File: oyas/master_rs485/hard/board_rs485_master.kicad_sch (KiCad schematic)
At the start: 0 parts

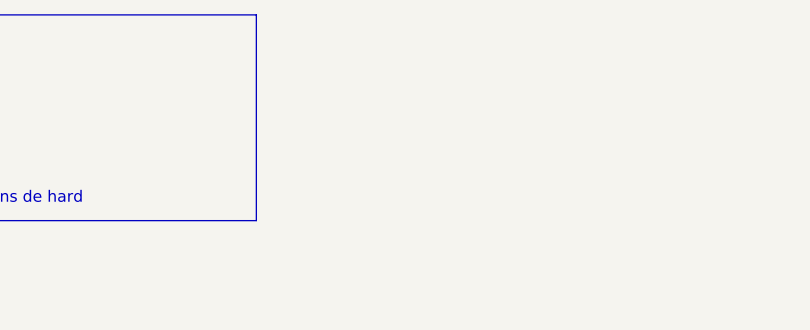
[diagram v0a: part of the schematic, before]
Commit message: MAJ correction limitation du courant de base des pnp (Pwr Wifi et LEDs)
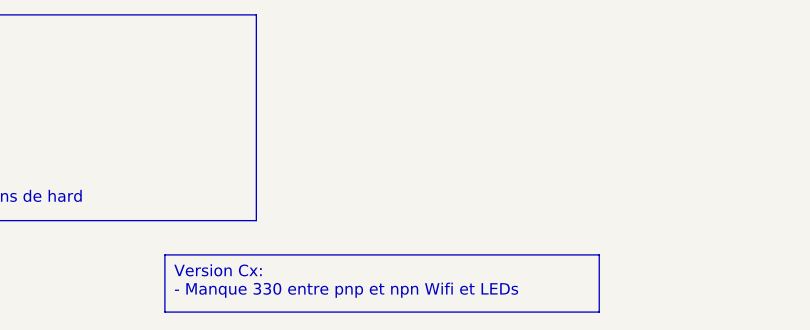
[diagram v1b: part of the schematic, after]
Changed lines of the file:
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@@
   (title_block
     (title "Commande des OYA - Maître RS485")
-    (date "2024-05-06")
-    (rev "B0")
+    (date "2025-05-25")
+    (rev "C0")
     (company "BPC")
     (comment 1 "Extension Wifi (ESP01)")
@@
     (stroke (width 0) (type default))
     (fill (type none))
+    (effects (font (size 1.27 1.27)) (justify left top))
+  )
+  (text_box "Version Cx:\n- Manque 330 entre pnp et npn Wifi et LEDs"
+    (at 127 189.23 0) (size 48.26 6.35)
+    (stroke (width 0) (type default))
+    (fill (type none))
